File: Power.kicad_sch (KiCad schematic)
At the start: 26 parts, among them J6 Conn_01x02, Q1 AO3401A, Q3 CSD16301Q2, Q4 CSD16301Q2, U10 BQ40Z50RSMT, U4 BQ29700, U6 TPS2116DRL, U7 TPS61033DRLR, U9 BQ25798

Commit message: revise efuse, add bat
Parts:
- added U5: TPS259474ARPWR, easyeda2kicad:VQFN-10_L2.0-W2.0-P0.45-TL, symbol easyeda2kicad:TPS259474ARPWR
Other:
- moved on the sheet: U10
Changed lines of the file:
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@@
 	(symbol
 		(lib_id "BQ40Z50RSMT:BQ40Z50RSMT")
-		(at 132.08 151.13 0)
+		(at 80.01 147.32 0)
 		(unit 1)
 		(body_style 1)
@@
 		(fields_autoplaced yes)
 		(property "Reference" "U10"
-			(at 132.08 105.41 0)
+			(at 80.01 101.6 0)
 			(show_name no)
 			(do_not_autoplace no)
@@
 		)
 		(property "Value" "BQ40Z50RSMT"
-			(at 132.08 107.95 0)
+			(at 80.01 104.14 0)
 			(show_name no)
 			(do_not_autoplace no)
@@
 		)
 		(property "Footprint" "BQ40Z50RSMT:QFN40P400X400X100-33N"
-			(at 132.08 151.13 0)
+			(at 80.01 147.32 0)
 			(hide yes)
 			(show_name no)
@@
 		)
 		(property "Datasheet" ""
-			(at 132.08 151.13 0)
+			(at 80.01 147.32 0)
 			(hide yes)
 			(show_name no)
@@
 		)
 		(property "Description" "1-4 series Li-ion battery pack manager | battery fuel (gas) gauge"
-			(at 132.08 151.13 0)
+			(at 80.01 147.32 0)
 			(hide yes)
 			(show_name no)
@@
 		)
 		(property "MF" "Texas Instruments"
-			(at 132.08 151.13 0)
+			(at 80.01 147.32 0)
 			(hide yes)
 			(show_name no)
@@
 		)
 		(property "MAXIMUM_PACKAGE_HEIGHT" "1.00mm"
-			(at 132.08 151.13 0)
+			(at 80.01 147.32 0)
 			(hide yes)
 			(show_name no)
@@
 		)
 		(property "Package" "VQFN-32 Texas Instruments"
-			(at 132.08 151.13 0)
+			(at 80.01 147.32 0)
 			(hide yes)
 			(show_name no)
@@
 		)
 		(property "Price" "None"
-			(at 132.08 151.13 0)
+			(at 80.01 147.32 0)
 			(hide yes)
 			(show_name no)
@@
 		)
 		(property "Check_prices" "https://www.snapeda.com/parts/BQ40Z50RSMT/Texas+Instruments/view-part/?ref=eda"
-			(at 132.08 151.13 0)
+			(at 80.01 147.32 0)
 			(hide yes)
 			(show_name no)
@@
 		)
 		(property "STANDARD" "IPC-7351B"
-			(at 132.08 151.13 0)
+			(at 80.01 147.32 0)
 			(hide yes)
 			(show_name no)
@@
 		)
 		(property "PARTREV" "4219108/B 08/2019"
-			(at 132.08 151.13 0)
+			(at 80.01 147.32 0)
 			(hide yes)
 			(show_name no)
@@
 		)
 		(property "SnapEDA_Link" "https://www.snapeda.com/parts/BQ40Z50RSMT/Texas+Instruments/view-part/?ref=snap"
-			(at 132.08 151.13 0)
+			(at 80.01 147.32 0)
 			(hide yes)
 			(show_name no)
@@
 		)
 		(property "MP" "BQ40Z50RSMT"
-			(at 132.08 151.13 0)
+			(at 80.01 147.32 0)
 			(hide yes)
 			(show_name no)
@@
 		)
 		(property "Availability" "In Stock"
-			(at 132.08 151.13 0)
+			(at 80.01 147.32 0)
 			(hide yes)
 			(show_name no)
@@
 		)
 		(property "MANUFACTURER" "Texas Instruments"
-			(at 132.08 151.13 0)
+			(at 80.01 147.32 0)
 			(hide yes)
 			(show_name no)
@@
 					(unit 1)
 				)
+			)
+		)
+	)
+	(symbol
+		(lib_id "easyeda2kicad:TPS259474ARPWR")
+		(at 199.39 140.97 0)
+		(unit 1)
+		(body_style 1)
+		(exclude_from_sim no)
+		(in_bom yes)
+		(on_board yes)
+		(in_pos_files yes)
+		(dnp no)
+		(fields_autoplaced yes)
+		(property "Reference" "U5"
+			(at 200.025 151.13 0)
+			(show_name no)
+			(do_not_autoplace no)
+			(effects
+				(font
+					(size 1.27 1.27)
+				)
+			)
+		)
+		(property "Value" "TPS259474ARPWR"
+			(at 200.025 153.67 0)
+			(show_name no)
+			(do_not_autoplace no)
+			(effects
+				(font
+					(size 1.27 1.27)
+				)
+			)
+		)
+		(property "Footprint" "easyeda2kicad:VQFN-10_L2.0-W2.0-P0.45-TL"
+			(at 199.39 153.67 0)
+			(hide yes)
+			(show_name no)
+			(do_not_autoplace no)
+			(effects
+				(font
+					(size 1.27 1.27)
+				)
+			)
+		)
+		(property "Datasheet" "https://www.lcsc.com/datasheet/C3662807.pdf"
+			(at 199.39 156.21 0)
+			(hide yes)
+			(show_name no)
+			(do_not_autoplace no)
+			(effects
+				(font
+					(size 1.27 1.27)
+				)
+			)
+		)
+		(property "Description" ""
+			(at 199.39 140.97 0)
+			(hide yes)
+			(show_name no)
+			(do_not_autoplace no)
+			(effects
+				(font
+					(size 1.27 1.27)
+				)
+			)
+		)
+		(property "Manufacturer" "TI(德州仪器)"
+			(at 199.39 158.75 0)
+			(hide yes)
+			(show_name no)
+			(do_not_autoplace no)
+			(effects
+				(font
+					(size 1.27 1.27)
+				)
+			)
+		)
+		(property "MPN" "TPS259474ARPWR"
+			(at 199.39 161.29 0)
+			(hide yes)
+			(show_name no)
+			(do_not_autoplace no)
+			(effects
+				(font
+					(size 1.27 1.27)
+				)
+			)
+		)
+		(property "LCSC Part" "C3662807"
+			(at 199.39 163.83 0)
+			(hide yes)
+			(show_name no)
+			(do_not_autoplace no)
+			(effects
+				(font
+					(size 1.27 1.27)
+				)
+			)
+		)
+		(pin "5"
+		)
+		(pin "10"
+		)
+		(pin "1"
+		)
+		(pin "6"
+		)
+		(pin "3"
+		)
+		(pin "4"
+		)
+		(pin "8"
+		)
+		(pin "9"
+		)
+		(pin "2"
+		)
+		(pin "7"
+		)
+		(instances
+			(project "meshtastic"
+				(path "/fe9d4a31-2311-442f-997c-52ad8ca5cfe9/394887e0-c5eb-45fe-a43b-ed65e2bd0661"
+					(reference "U5")
+					(unit 1)
+				)

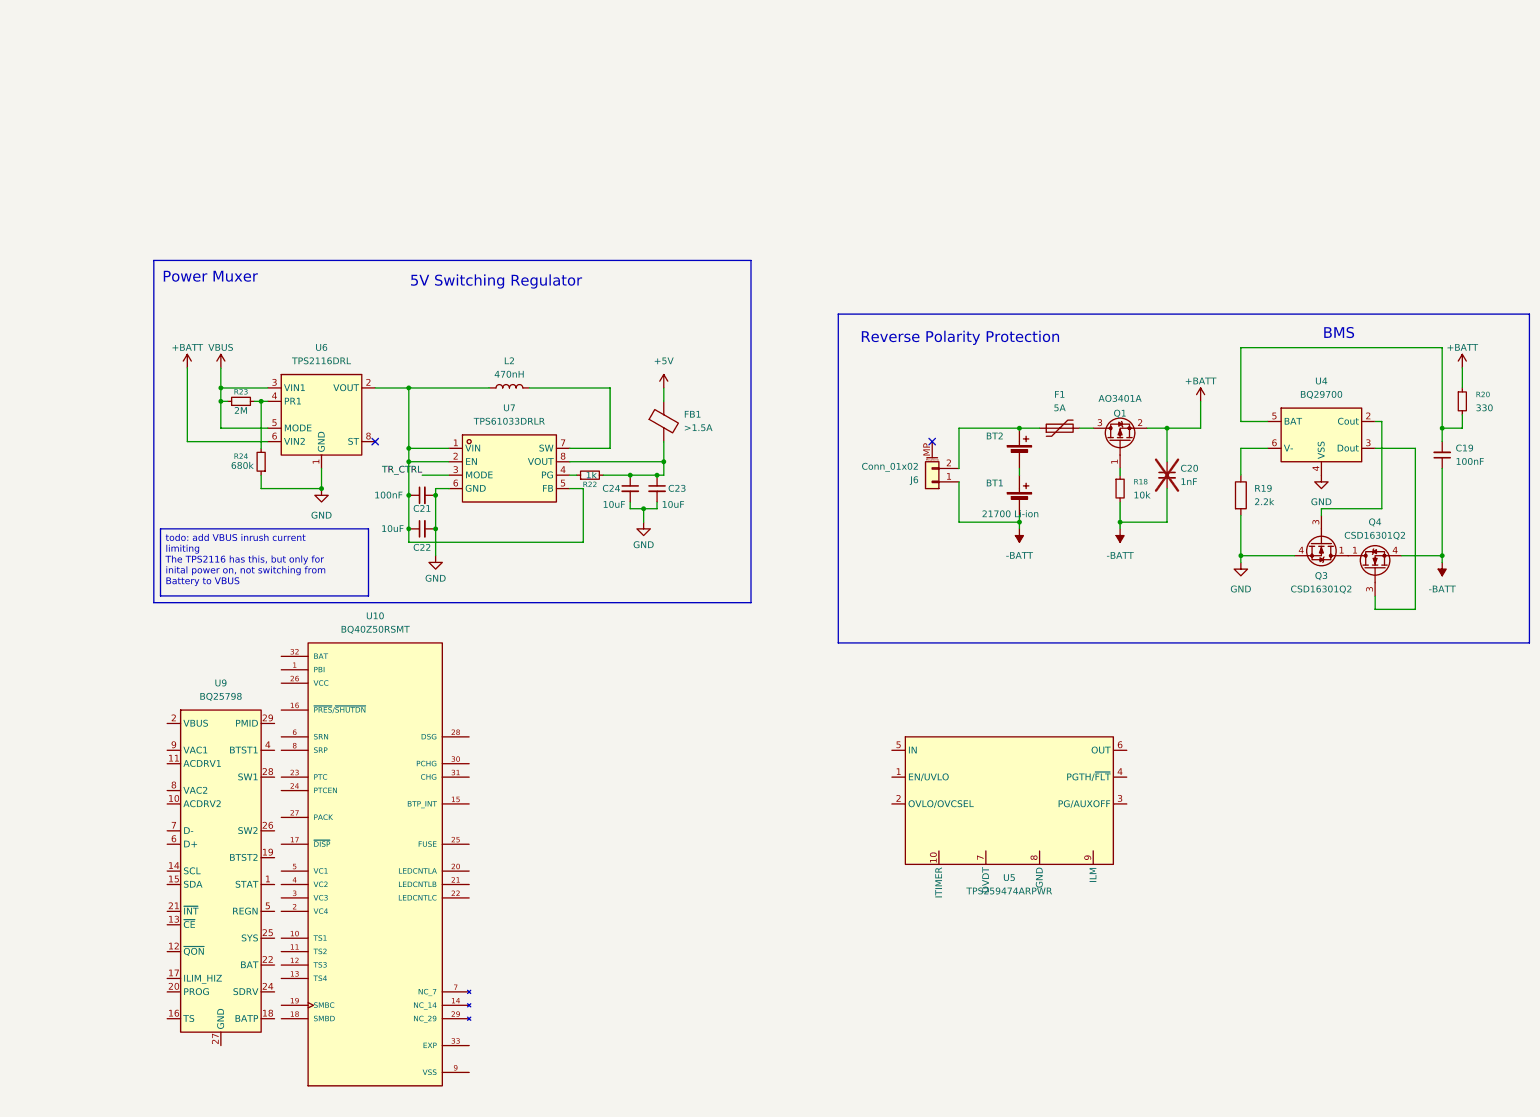
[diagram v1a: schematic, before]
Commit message: add BMS and charge controller!
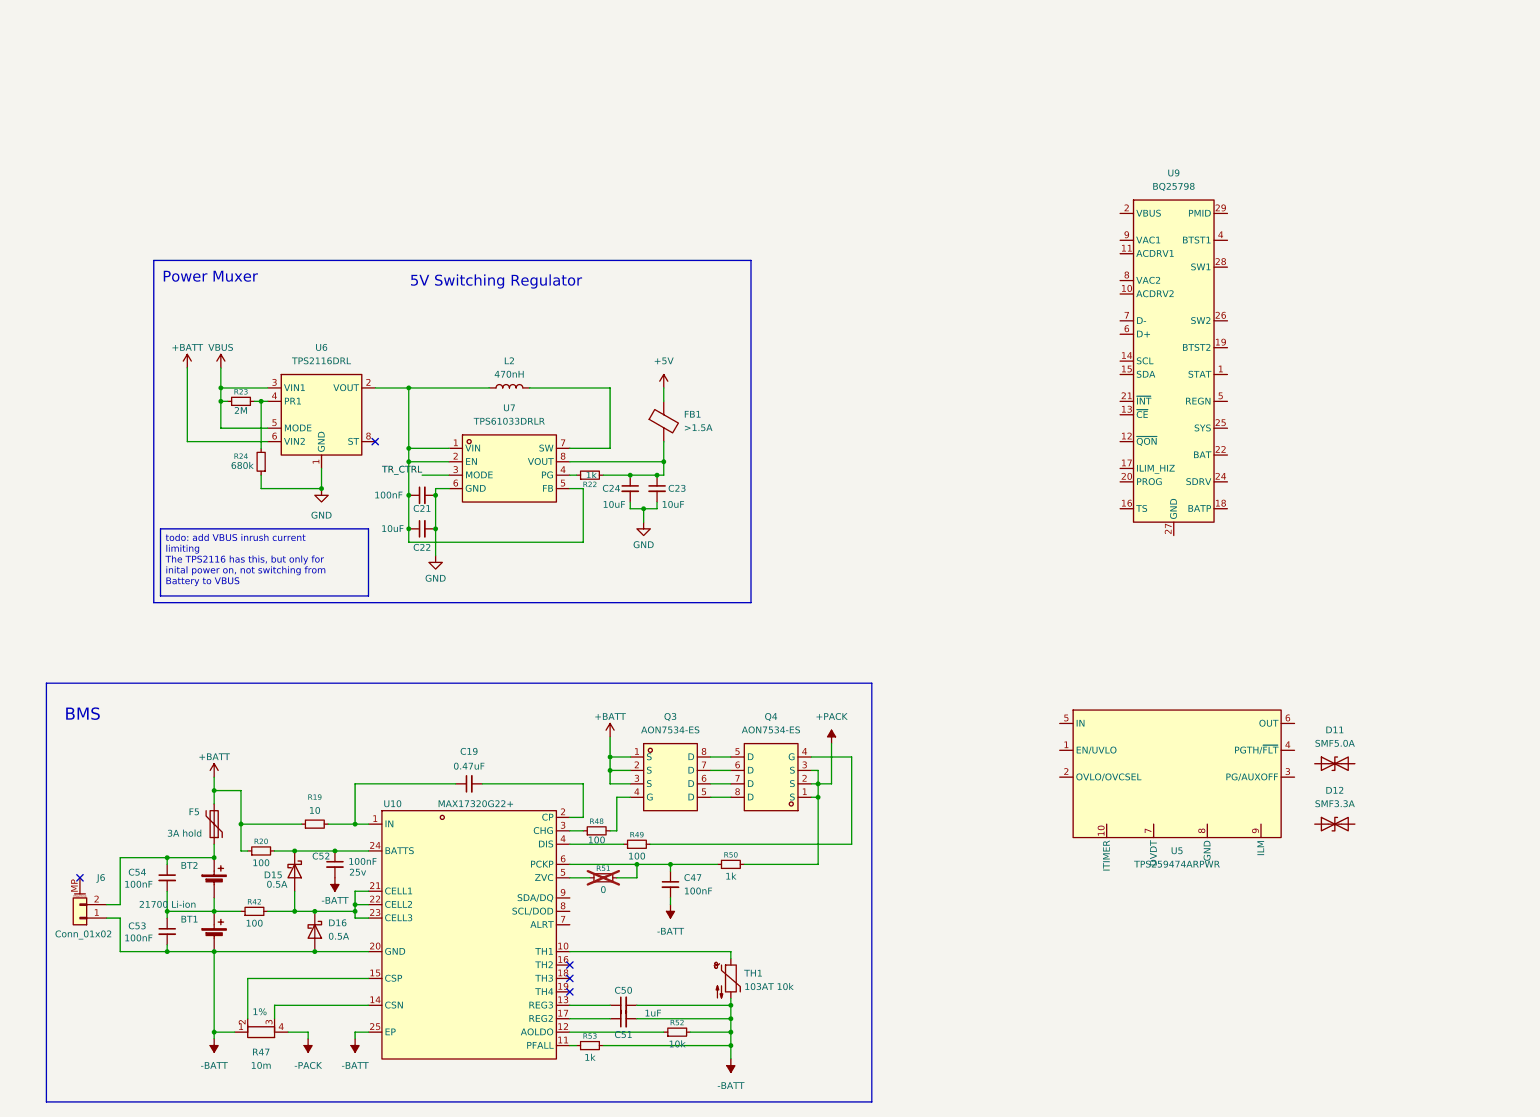
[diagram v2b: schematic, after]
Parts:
- removed C20: 1nF, Capacitor_SMD:C_0402_1005Metric, symbol Device:C_Small
- removed F1: 5A, symbol Device:Polyfuse
- removed Q1: AO3401A, Package_TO_SOT_SMD:SOT-23, symbol Transistor_FET:AO3401A
- removed Q3, Q4: CSD16301Q2, Package_SON:Texas_DQK, symbol Transistor_FET:CSD16301Q2
- removed R18: 10k, Resistor_SMD:R_0402_1005Metric, symbol Device:R_Small
- removed R19: 2.2k, Resistor_SMD:R_0402_1005Metric, symbol Device:R
- removed U10: BQ40Z50RSMT, BQ40Z50RSMT:QFN40P400X400X100-33N, symbol BQ40Z50RSMT:BQ40Z50RSMT
- removed U4: BQ29700, Package_SON:WSON-6_1.5x1.5mm_P0.5mm, symbol Battery_Management:BQ297xy
- added C47, C52, C53, C54: 100nF, symbol Device:C_Small
- added C50, C51: 1uF, Capacitor_SMD:C_0402_1005Metric, symbol Device:C_Small
- added D11: SMF5.0A, symbol Device:D_TVS
- added D12: SMF3.3A, symbol Device:D_TVS
- added D15, D16: 0.5A, symbol Device:D_Schottky
- added F5: 3A hold, symbol Device:Polyfuse
- added Q3, Q4: AON7534-ES, easyeda2kicad:PQFN-8_L3.1-W3.1-P0.65-LS3.3-BL, symbol easyeda2kicad:AON7534-ES
- added R19: 10, symbol Device:R_Small
- added R42, R48, R49: 100, symbol Device:R_Small
- added R47: 10m, symbol Device:R_Shunt
- added R50, R53: 1k, symbol Device:R_Small
- added R51: 0, symbol Device:R_Small
- added R52: 10k, symbol Device:R_Small
- added TH1: 103AT 10k, symbol Device:Thermistor_NTC
- added U10: MAX17320G22+, easyeda2kicad:QFN-24_L4.0-W4.0-P0.50-BL-EP2.6, symbol easyeda2kicad:MAX17320G22+
- C19: value 100nF -> 0.47uF; footprint Capacitor_SMD:C_0402_1005Metric -> (none)
- R20: value 330 -> 100; footprint Resistor_SMD:R_0402_1005Metric -> (none)
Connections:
- net +BATT: now also F5.2, Q3.1 (S), Q3.2 (S), Q3.3 (S), R19.1
- net -BATT: now also C47.2, C50.2, C51.2, C52.2, C53.2, D16.2 (A), R47.1, R52.2, R53.2, TH1.2, U10.20 (GND), U10.25 (EP); no longer C19.1
- net at R20.2: now also C52.1, D15.1 (K), U10.24 (BATTS); no longer C19.2
- net at BT2.1 (+), J6.2 (Pin_2): now also C54.1, F5.1
- net at BT1.1 (+), BT2.2 (-): now also C53.1, C54.2, R42.1
- new net: D15.2 (A), D16.1 (K), R42.2, U10.21 (CELL1), U10.22 (CELL2), U10.23 (CELL3)
- new net: R48.1, U10.3 (CHG)
- new net: Q3.4 (G), R48.2
- new net: R53.1, U10.11 (PFALL)
- new net: C19.1, R19.2, U10.1 (IN)
- new net: C19.2, U10.2 (CP)
- new net: Q3.5 (D), Q4.8 (D)
- new net: Q3.6 (D), Q4.7 (D)
- new net: Q3.7 (D), Q4.6 (D)
- new net: Q3.8 (D), Q4.5 (D)
- new net: R47.2, U10.15 (CSP)
- new net: R47.3, U10.14 (CSN)
- new net: C51.1, U10.17 (REG2)
- new net: C47.1, R50.1, R51.2, U10.6 (PCKP)
- new net: R49.1, U10.4 (DIS)
- new net: Q4.4 (G), R49.2
- new net: R52.1, U10.12 (AOLDO)
- new net: C50.1, U10.13 (REG3)
- new net: TH1.1, U10.10 (TH1)
- new net: R51.1, U10.5 (ZVC)
- new net +PACK: Q4.1 (S), Q4.2 (S), Q4.3 (S), R50.2
- new net -PACK: R47.4
- no-connect marks 2 -> 5
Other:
- note removed: "Reverse Polarity Protection"
- moved on the sheet: U5, U9

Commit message: small update
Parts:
- removed C54: 100nF, symbol Device:C_Small
- added C20: 22uF, Capacitor_SMD:C_0805_2012Metric, symbol Device:C_Small
- added C55, C56, C57, C58, C59: 100nF, symbol Device:C_Small
- C19: Voltage Rating (none) -> >=25v
- C53: value 100nF -> 1uF
- Q3, Q4: value AON7534-ES -> AON7534; LCSC Part C23083862 -> C115844; MPN AON7534-ES -> AON7534; Manufacturer ElecSuper(静芯) -> (none)
- R20: value 100 -> 150
- R42: value 100 -> 150; footprint (none) -> Resistor_SMD:R_0805_2012Metric
- R51: value 0 -> 330
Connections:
- net -PACK is gone; now on net GND: R47.4
- net +BATT: now also C56.1, C59.1; no longer R19.1, R20.1, U6.6 (VIN2)
- net +PACK: now also C47.1, R51.2, U6.6 (VIN2), C59.2
- net -BATT: now also C20.2, C55.2, C57.2
- net at BT1.1 (+), BT2.2 (-), R42.1: no longer C53.1
- net at C52.1, D15.1 (K), R20.2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: now also C58.1
- net at D15.2 (A), D16.1 (K), R42.2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: now also C57.1, C58.2
- net at Q3.4 (G), R48.2: now also C56.2
- net at BT2.1 (+), F5.1, J6.2 (Pin_2): now also C53.1, R19.1, R20.1, C20.1
- net at C19.1, R19.2, U10.1 (IN): now also C55.1
- net at R50.1, U10.6 (PCKP): no longer C47.1, R51.2
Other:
- moved on the sheet: BT1, C47, C52, C53, D15, D16, F5, J6, R19, R20, R42, R47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

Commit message: update bms schematic, minor changes to rest
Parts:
- added C54: 0.47uF, Capacitor_SMD:C_0402_1005Metric, symbol Device:C_Small
- added C60, C61, C62, C63: 10uF, Capacitor_SMD:C_0805_2012Metric, symbol Device:C_Small
- added R54: 10k, symbol Device:R_Small
- added TH2: 103AT 10k, symbol Device:Thermistor_NTC
- added TP1: REG3, symbol Connector:TestPoint_Probe
- added TP3: R_SENSE_SHUNT, TestPoint:TestPoint_2Pads_Pitch2.54mm_Drill0.8mm, symbol Connector:TestPoint_2Pole
- added TP4: IN_CP, TestPoint:TestPoint_2Pads_Pitch2.54mm_Drill0.8mm, symbol Connector:TestPoint_2Pole
- C19: Voltage Rating >=25v -> 25V
- C20, C47, C53, C59: Voltage Rating (none) -> 50V
- C50: value 1uF -> 0.47uF; Voltage Rating (none) -> 25V
- C51: value 1uF -> 0.47uF; Voltage Rating (none) -> 16V
- C52, C58: Voltage Rating 25v -> 50V
- C55: value 100nF -> 1uF; Voltage Rating 25v -> 50V
- C56: Voltage Rating 25v -> 25V
- C57: Voltage Rating (none) -> 25V
- FB1: LCSC Part C14709 -> (none)
- R20: footprint (none) -> Resistor_SMD:R_1206_3216Metric
- R42: footprint Resistor_SMD:R_0805_2012Metric -> Resistor_SMD:R_1206_3216Metric; Power Rating (none) -> 0.25W
- R51: value 330 -> 330 0.75w; footprint (none) -> Resistor_SMD:R_2010_5025Metric
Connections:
- net +PACK: now also C60.1, C61.1, C62.1, C63.1
- net -BATT: now also C54.2, TH2.2, TP3.1
- net GND: now also C60.2, C61.2, C62.2, C63.2, TP3.2
- net at C52.1, C58.1, D15.1 (K)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: now also U10.22 (CELL2), U10.23 (CELL3)
- net at C57.1, C58.2, D15.2 (A)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: no longer U10.22 (CELL2), U10.23 (CELL3)
- net at C19.1, C55.1, R19.2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: now also TP4.1
- net at C19.2, U10.2 (CP): now also TP4.2
- net at R52.1, U10.12 (AOLDO): now also C54.1
- net at C50.1, U10.13 (REG3): now also TP1.1
- net at U10.16 (TH2): now also TH2.1
- net at U10.7 (ALRT): now also R54.1
- new net +3V3: R54.2
- no-connect marks 5 -> 4
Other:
- note added: "Capacitors voltage ratings specified - use XR7/C0G"
- moved on the sheet: R49, U5
